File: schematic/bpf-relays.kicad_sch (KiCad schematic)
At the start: 24 parts, among them U12 ULN2803A, U13 74HC238, U14 L78L33

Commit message: Add /TX Common/ schematic sheet
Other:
- note added: "see /RX/"
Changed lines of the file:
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@@
+    (effects (font (size 1.27 1.27)) (justify left bottom))
+  )
+  (text "see /RX/" (at 271.78 28.575 0)
     (effects (font (size 1.27 1.27)) (justify left bottom))
   )

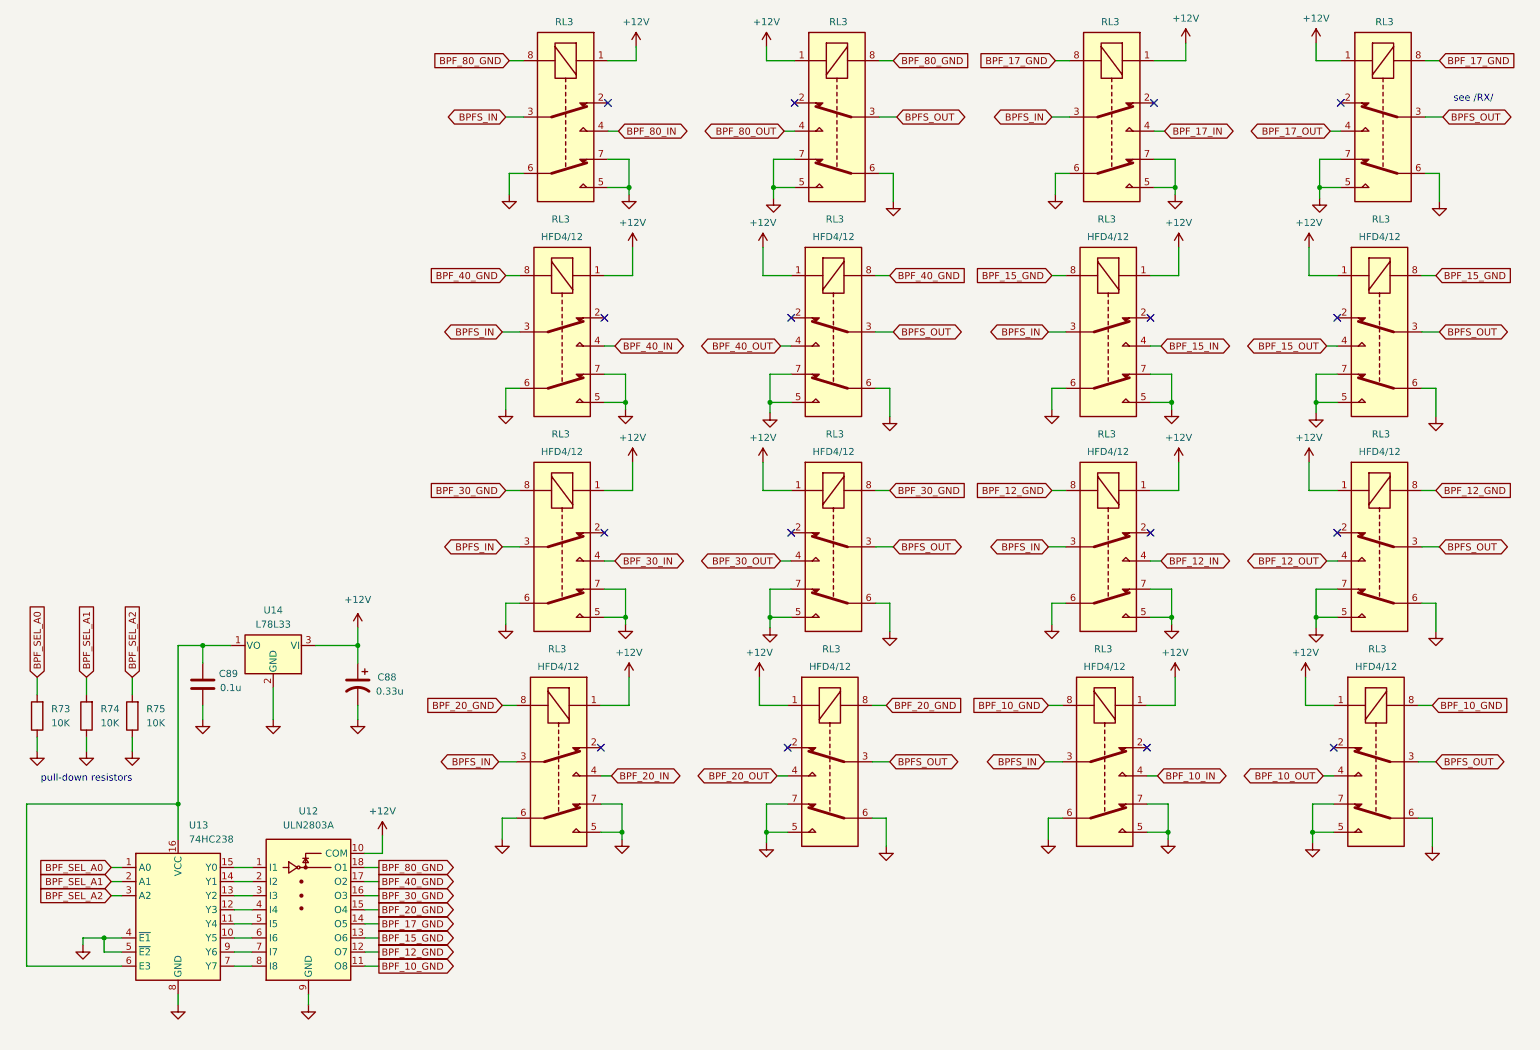
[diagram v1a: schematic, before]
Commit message: Connect relay contact groups in parallel where appropriate
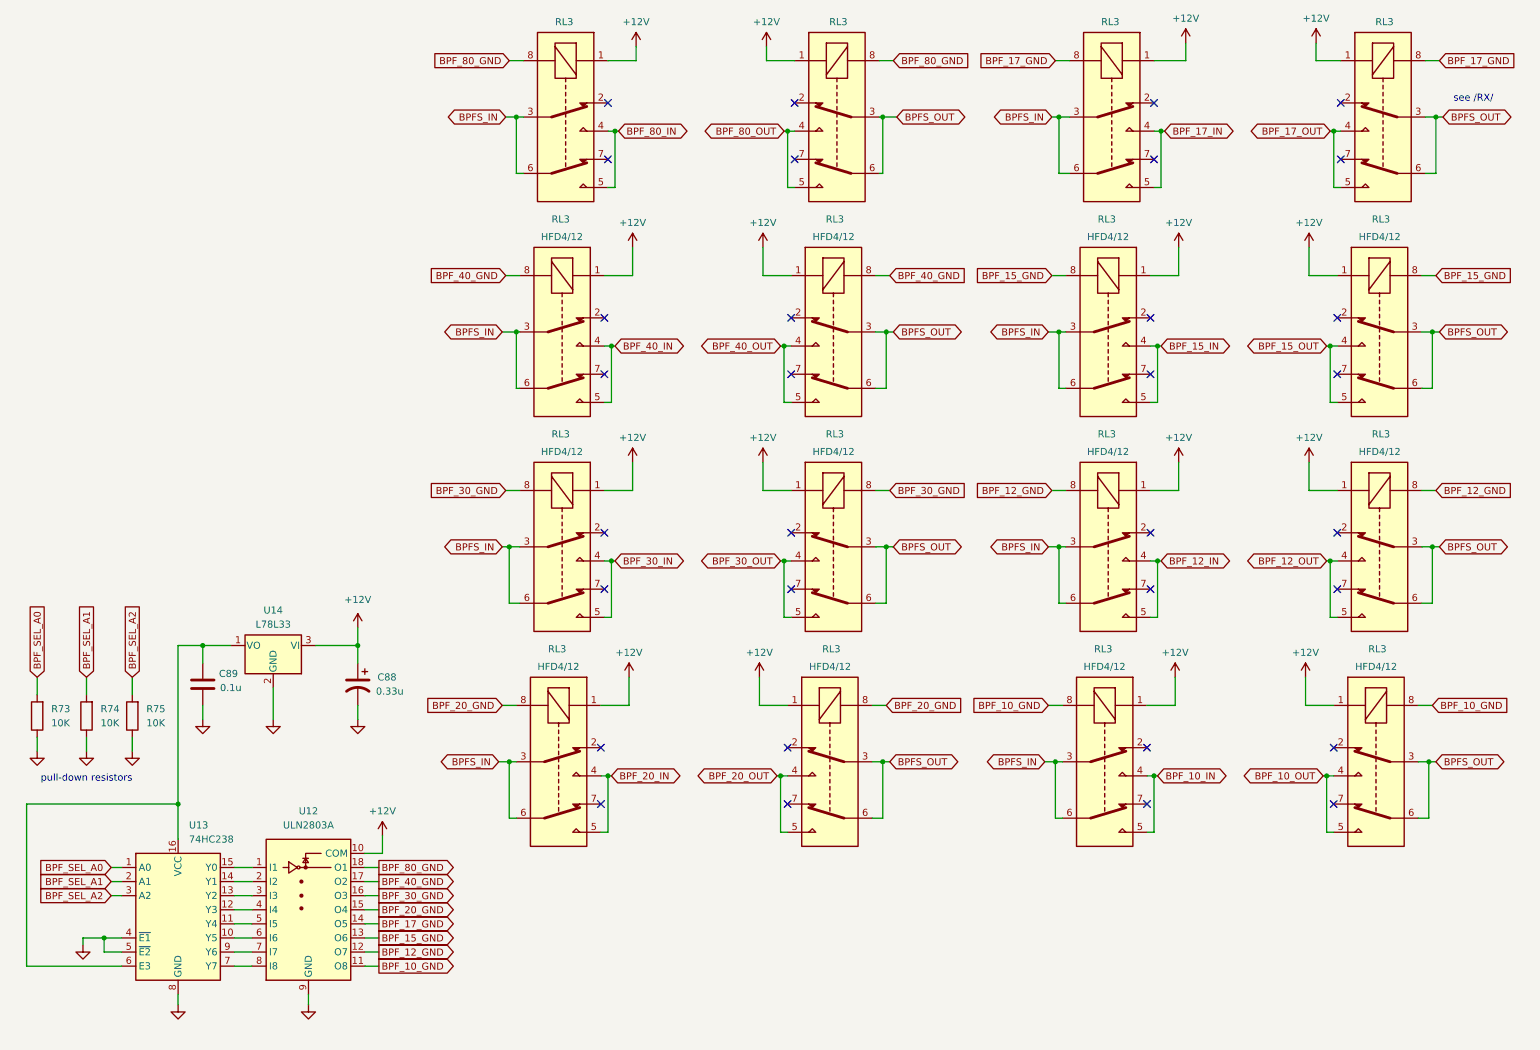
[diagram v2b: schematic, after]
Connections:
- net BPFS_IN: now also RL3.6, RL3.6, RL3.6, RL3.6, RL3.6, RL3.6, RL3.6, RL3.6
- net BPFS_OUT: now also RL3.6, RL3.6, RL3.6, RL3.6, RL3.6, RL3.6, RL3.6, RL3.6
- net BPF_10_IN: now also RL3.5
- net BPF_10_OUT: now also RL3.5
- net BPF_12_IN: now also RL3.5
- net BPF_12_OUT: now also RL3.5
- net BPF_15_IN: now also RL3.5
- net BPF_15_OUT: now also RL3.5
- net BPF_17_IN: now also RL3.5
- net BPF_17_OUT: now also RL3.5
- net BPF_20_IN: now also RL3.5
- net BPF_20_OUT: now also RL3.5
- net BPF_30_IN: now also RL3.5
- net BPF_30_OUT: now also RL3.5
- net BPF_40_IN: now also RL3.5
- net BPF_40_OUT: now also RL3.5
- net BPF_80_IN: now also RL3.5
- net BPF_80_OUT: now also RL3.5
- net GND: no longer RL3.5, RL3.5, RL3.5, RL3.5, RL3.5, RL3.5, RL3.5, RL3.5, RL3.5, RL3.5, RL3.5, RL3.5, RL3.5, RL3.5, RL3.5, RL3.5, RL3.6, RL3.6, RL3.6, RL3.6, RL3.6, RL3.6, RL3.6, RL3.6, RL3.6, RL3.6, RL3.6, RL3.6, RL3.6, RL3.6, RL3.6, RL3.6, RL3.7, RL3.7, RL3.7, RL3.7, RL3.7, RL3.7, RL3.7, RL3.7, RL3.7, RL3.7, RL3.7, RL3.7, RL3.7, RL3.7, RL3.7, RL3.7
- no-connect marks 16 -> 32

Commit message: Add diodes for BPF relays
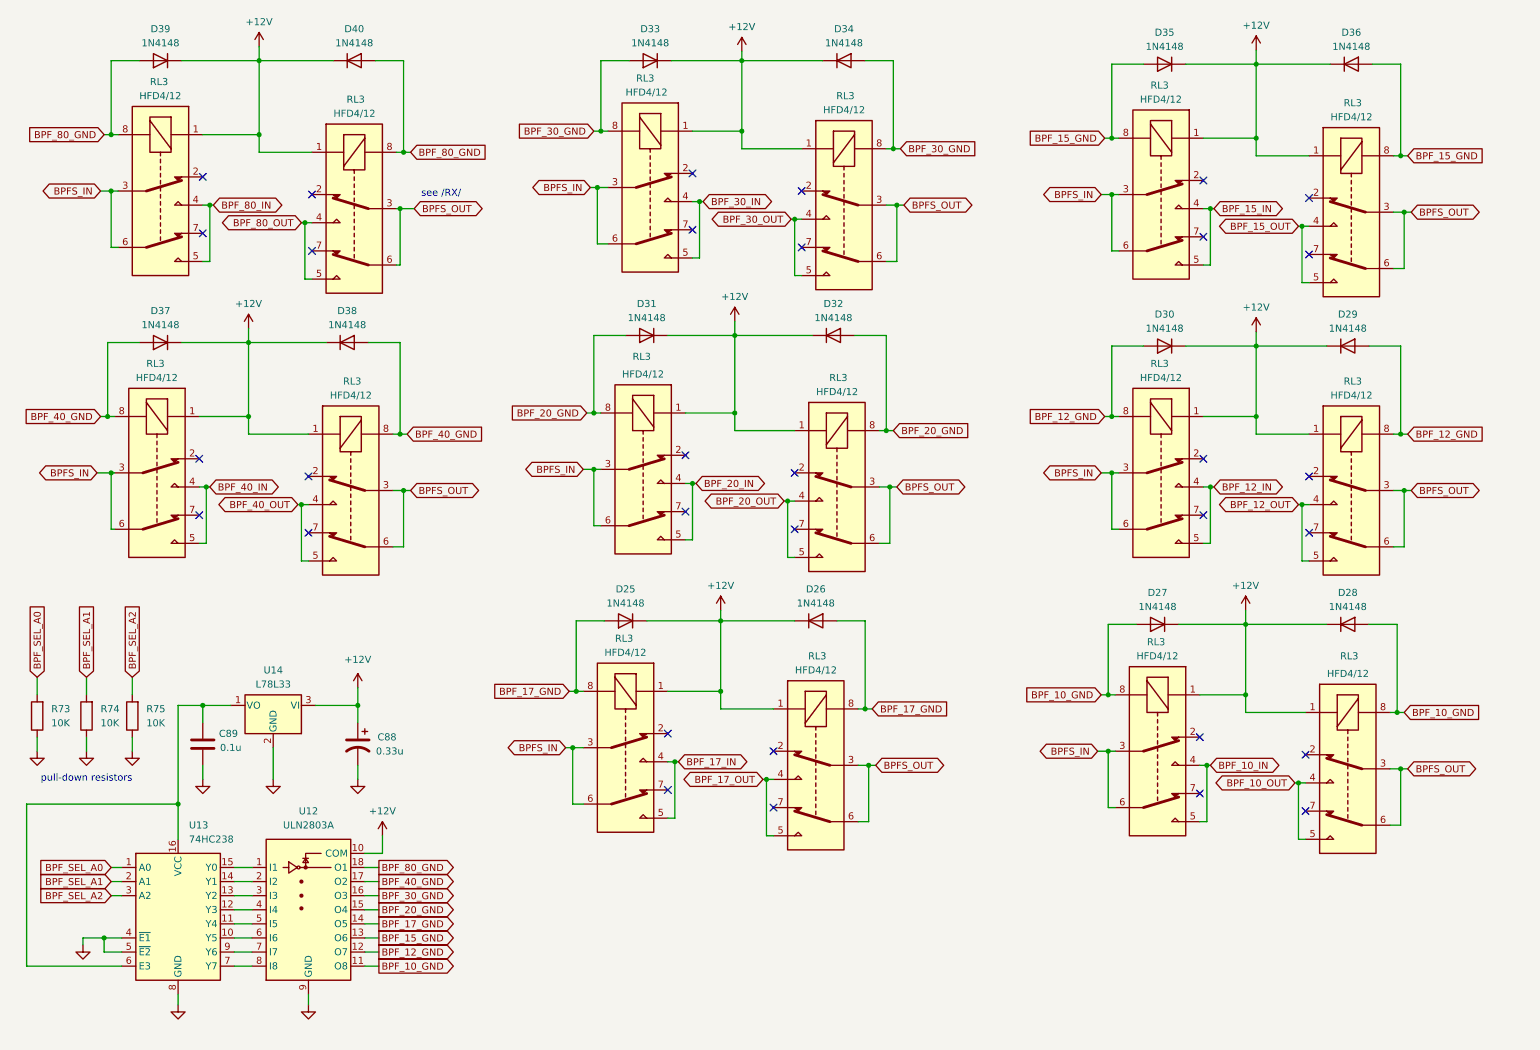
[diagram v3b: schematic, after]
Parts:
- added D25, D26, D27, D28, D29, D30, D31, D32, D33, D34, D35, D36, D37, D38, D39, D40: 1N4148, Diode_THT:D_DO-35_SOD27_P7.62mm_Horizontal, symbol Diode:1N4148
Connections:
- net +12V: now also D25.1 (K), D26.1 (K), D27.1 (K), D28.1 (K), D29.1 (K), D30.1 (K), D31.1 (K), D32.1 (K), D33.1 (K), D34.1 (K), D35.1 (K), D36.1 (K), D37.1 (K), D38.1 (K), D39.1 (K), D40.1 (K)
- net BPF_10_GND: now also D27.2 (A), D28.2 (A)
- net BPF_12_GND: now also D29.2 (A), D30.2 (A)
- net BPF_15_GND: now also D35.2 (A), D36.2 (A)
- net BPF_17_GND: now also D25.2 (A), D26.2 (A)
- net BPF_20_GND: now also D31.2 (A), D32.2 (A)
- net BPF_30_GND: now also D33.2 (A), D34.2 (A)
- net BPF_40_GND: now also D37.2 (A), D38.2 (A)
- net BPF_80_GND: now also D39.2 (A), D40.2 (A)
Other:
- moved on the sheet: C88, C89, RL3, U14

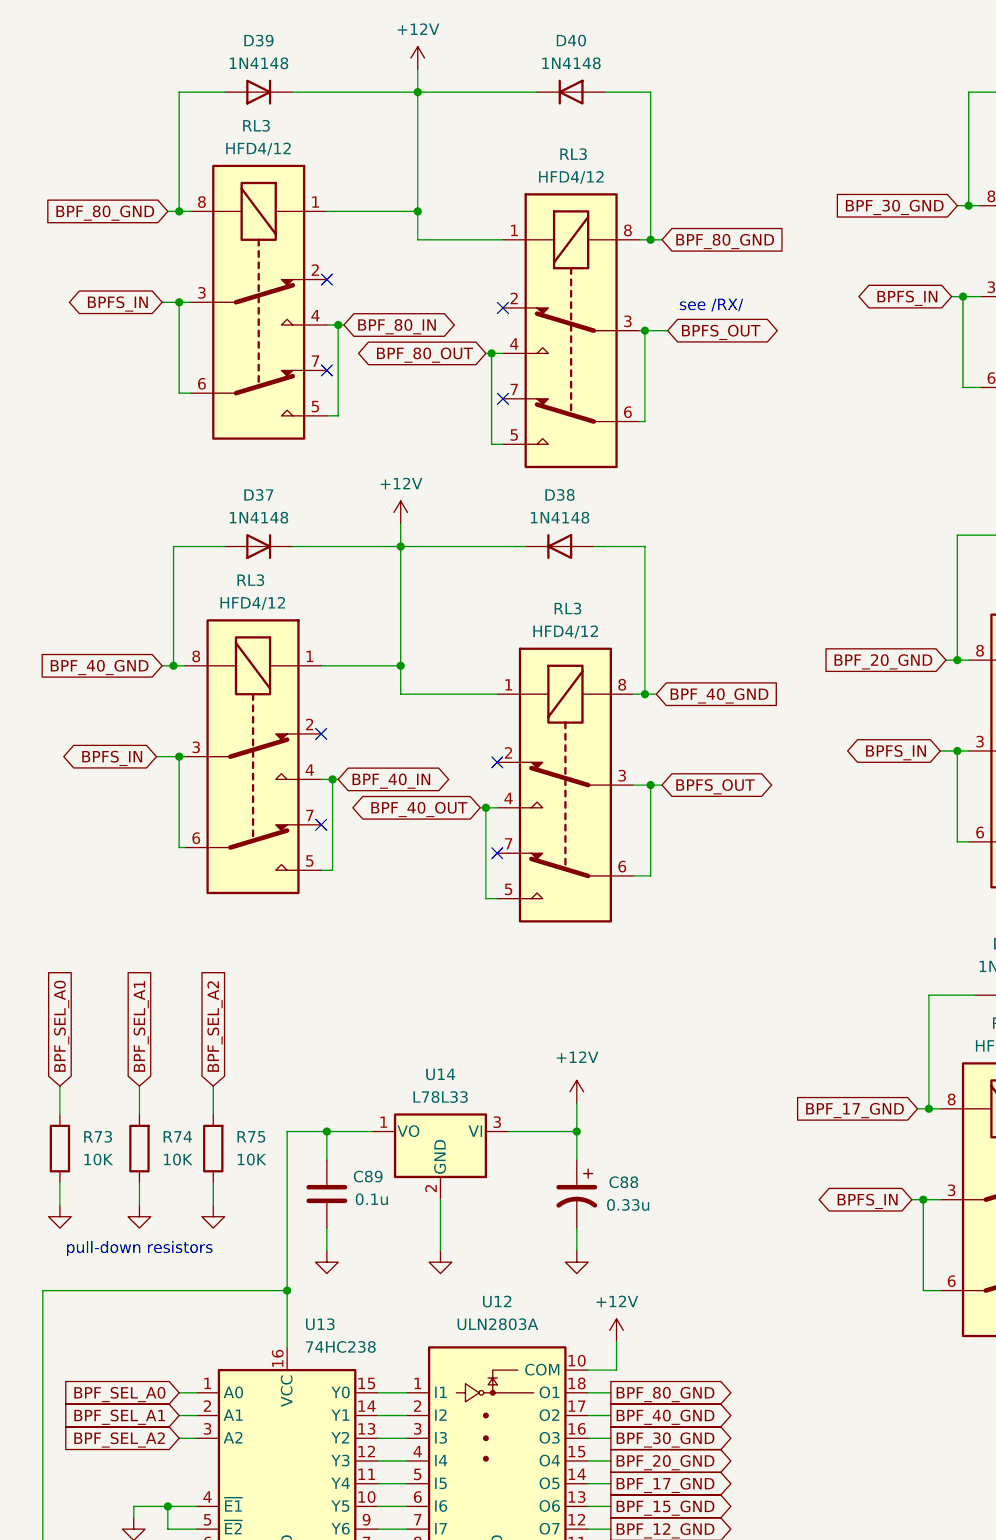
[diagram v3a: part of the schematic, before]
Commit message: Schematic: minor changes
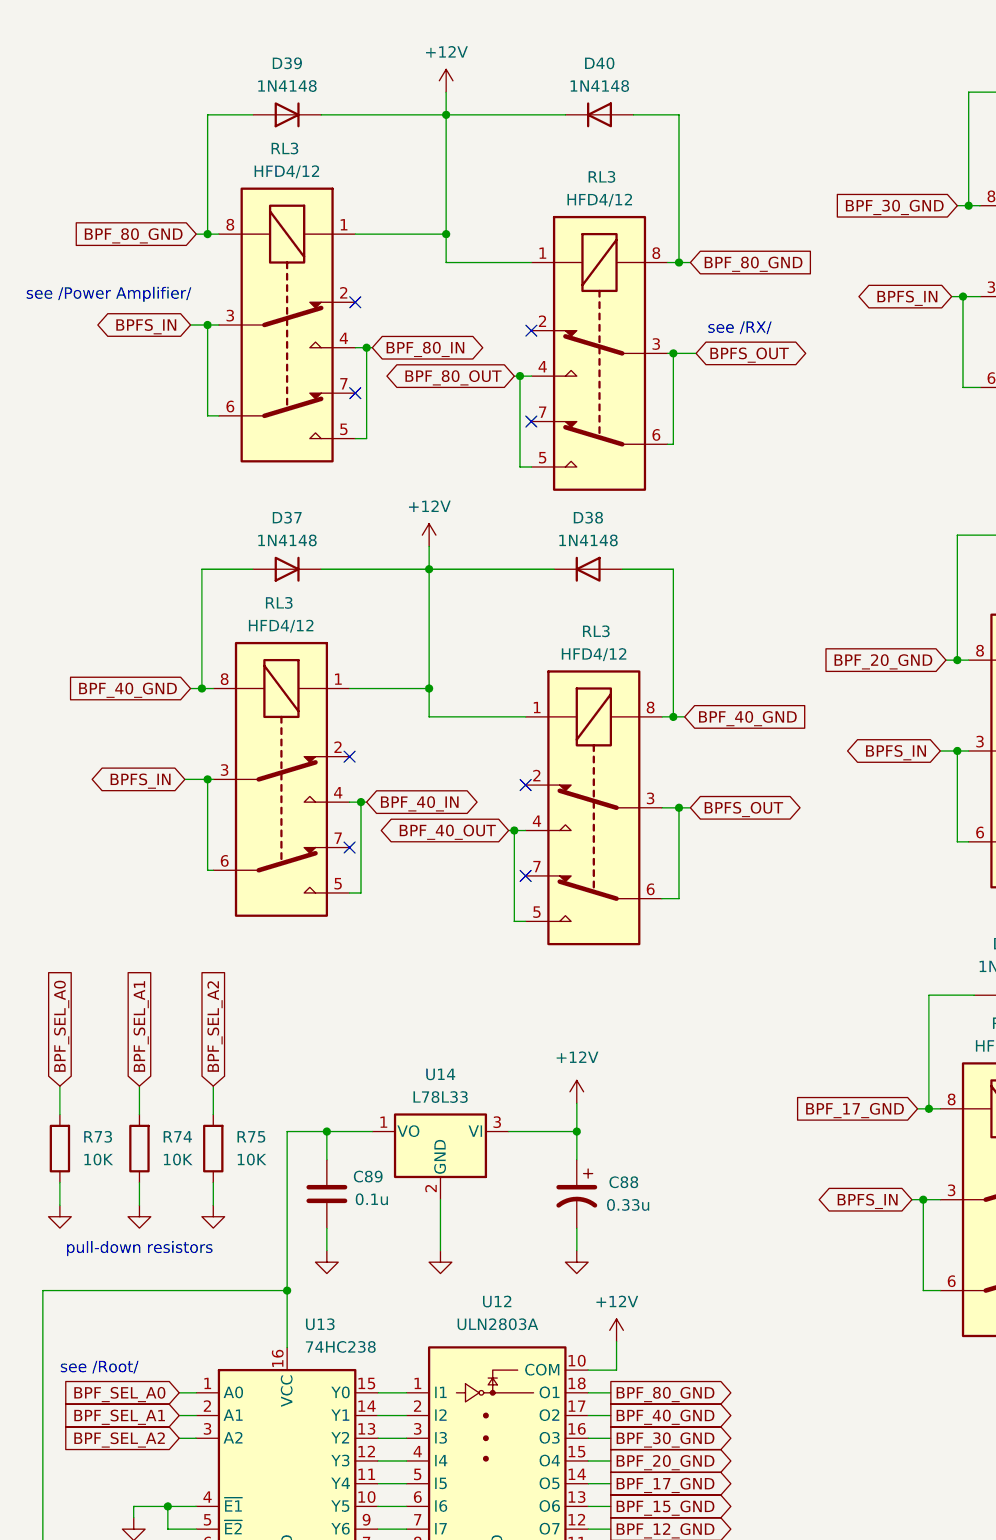
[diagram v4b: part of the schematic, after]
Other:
- note added: "see /Power Amplifier/"
- note added: "see /Root/"
- moved on the sheet: D37, D38, D39, D40, RL3
